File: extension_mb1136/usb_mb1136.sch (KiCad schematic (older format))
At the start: 21 parts, among them J1 Conn_01x03, J2 Conn_01x03, Q1 S9013, U1 STMPS2151MTR, U2 USBLC6-2

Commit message: update pcb
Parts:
- removed CNUSB_3: USB_B, Connector_USB:USB_B_OST_USB-B1HSxx_Horizontal, symbol Connector:USB_B
- added CNUSB_3: USB_BP, Connector_USB:USB_B_OST_USB-B1HSxx_Horizontal, symbol usb_connector_switch:USB_BP
- added D2: D, Diode_SMD:D_0805_2012Metric, symbol Device:D
- added SW1, SW2: USB_SEL, Connector_PinSocket_2.54mm:PinSocket_2x03_P2.54mm_Vertical, symbol usb_connector_switch:USB_SEL
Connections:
- net +5V: now also D2.1 (K)
- net GND: now also CNUSB_3.4 (GND), CNUSB_3.5 (Shield)
- net PA9 renamed VBUS
- new net: CNUSB_1.2 (D-), SW2.4
- new net: CNUSB_1.3 (D+), SW1.4
- new net: SW2.3, U2.4 (DMOUT)
- new net: SW1.3, U2.6 (DPOUT)
- new net: CNUSB_2.2 (D-), SW2.5
- new net: CNUSB_2.3 (D+), SW1.5
- new net: CNUSB_3.3 (D+), SW1.1
- new net: CNUSB_3.2 (D-), SW2.1
- new net: CNUSB_3.1 (VBUS), D2.2 (A)
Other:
- moved on the sheet: CNUSB_1, D1
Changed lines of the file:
@@
 L Connector:USB_OTG CNUSB_1
 U 1 1 5FBD271C
-P 10150 1900
-F 0 "CNUSB_1" H 9920 1889 50  0000 R CNN
-F 1 "USB_OTG" H 9920 1798 50  0000 R CNN
-F 2 "Connector_USB:USB_Micro-B_Molex-105017-0001" H 10300 1850 50  0001 C CNN
-F 3 " ~" H 10300 1850 50  0001 C CNN
-	1    10150 1900
+P 10150 1950
+F 0 "CNUSB_1" H 9920 1939 50  0000 R CNN
+F 1 "USB_OTG" H 9920 1848 50  0000 R CNN
+F 2 "Connector_USB:USB_Micro-B_Molex-105017-0001" H 10300 1900 50  0001 C CNN
+F 3 " ~" H 10300 1900 50  0001 C CNN
+	1    10150 1950
 	-1   0    0    -1
 $EndComp
@@
 $EndComp
 Wire Wire Line
-	9200 3000 9200 2500
-Wire Wire Line
 	10150 3400 10150 3500
 Wire Wire Line
@@
 Connection ~ 9100 2100
 Wire Wire Line
-	9100 2100 9100 1700
+	9100 2100 9100 1750
 Wire Wire Line
 	9100 2800 9100 2100
@@
 	6150 4600 6150 4700
 $Comp
-L power:GND #PWR0101
+L power:GND #PWR0104
 U 1 1 5FFB903B
 P 6150 6500
-F 0 "#PWR0101" H 6150 6250 50  0001 C CNN
+F 0 "#PWR0104" H 6150 6250 50  0001 C CNN
 F 1 "GND" H 6155 6327 50  0000 C CNN
 F 2 "" H 6150 6500 50  0001 C CNN
@@
 Wire Wire Line
 	4650 3200 4950 3200
-Wire Wire Line
-	8200 3200 8200 2500
-Wire Wire Line
-	8200 2500 9200 2500
-Connection ~ 9200 2500
-Wire Wire Line
-	9200 2500 9200 1900
-Wire Wire Line
-	9400 4150 4650 4150
 $Comp
 L Device:D D1
 U 1 1 600DB0FD
-P 9400 4450
-F 0 "D1" V 9354 4530 50  0000 L CNN
-F 1 "ESDALC6V1-1U2" V 9445 4530 50  0000 L CNN
-F 2 "Diode_SMD:D_0201_0603Metric" H 9400 4450 50  0001 C CNN
-F 3 "~" H 9400 4450 50  0001 C CNN
-	1    9400 4450
+P 9700 4450
+F 0 "D1" V 9654 4530 50  0000 L CNN
+F 1 "ESDALC6V1-1U2" V 9745 4530 50  0000 L CNN
+F 2 "Diode_SMD:D_0201_0603Metric" H 9700 4450 50  0001 C CNN
+F 3 "~" H 9700 4450 50  0001 C CNN
+	1    9700 4450
 	0    1    1    0
 $EndComp
 Wire Wire Line
-	9400 4150 9400 4300
-Connection ~ 9400 4150
+	9700 4150 9700 4300
+Connection ~ 9700 4150
 $Comp
 L power:GND #PWR0114
 U 1 1 600E78F0
-P 9400 4700
-F 0 "#PWR0114" H 9400 4450 50  0001 C CNN
-F 1 "GND" H 9405 4527 50  0000 C CNN
-F 2 "" H 9400 4700 50  0001 C CNN
-F 3 "" H 9400 4700 50  0001 C CNN
-	1    9400 4700
-	1    0    0    -1
-$EndComp
-Wire Wire Line
-	9400 4600 9400 4700
-Wire Wire Line
-	9400 2100 9400 4150
-Wire Wire Line
-	6550 3200 8200 3200
-Wire Wire Line
-	6550 3400 8350 3400
+P 9700 4700
+F 0 "#PWR0114" H 9700 4450 50  0001 C CNN
+F 1 "GND" H 9705 4527 50  0000 C CNN
+F 2 "" H 9700 4700 50  0001 C CNN
+F 3 "" H 9700 4700 50  0001 C CNN
+	1    9700 4700
+	1    0    0    -1
+$EndComp
+Wire Wire Line
+	9700 4600 9700 4700
+Wire Wire Line
+	6550 3200 7950 3200
 $Comp
 L power:GND #PWR0115
@@
 Wire Wire Line
 	4650 3400 5650 3400
-Wire Wire Line
-	9300 2000 9300 2650
-Wire Wire Line
-	8350 3400 8350 2650
-Wire Wire Line
-	8350 2650 9300 2650
-Connection ~ 9300 2650
-Wire Wire Line
-	9300 2650 9300 3100
 Wire Wire Line
 	4650 2900 7850 2900
@@
 	1    0    0    -1
 $EndComp
-$Comp
-L Connector:USB_B CNUSB_3
-U 1 1 5FFEEA84
+Wire Wire Line
+	9800 3500 10150 3500
+Connection ~ 10150 3500
+$Comp
+L power:GND #PWR0105
+U 1 1 60077159
+P 10150 3600
+F 0 "#PWR0105" H 10150 3350 50  0001 C CNN
+F 1 "GND" H 10155 3427 50  0000 C CNN
+F 2 "" H 10150 3600 50  0001 C CNN
+F 3 "" H 10150 3600 50  0001 C CNN
+	1    10150 3600
+	1    0    0    -1
+$EndComp
+Wire Wire Line
+	9100 2800 9850 2800
+Wire Wire Line
+	9850 1050 9200 1050
+Wire Wire Line
+	9200 1050 9200 2450
+Wire Wire Line
+	9200 2450 8700 2450
+Wire Wire Line
+	9300 2550 8700 2550
+Wire Wire Line
+	9850 3000 8800 3000
+Wire Wire Line
+	8800 3000 8800 2650
+Wire Wire Line
+	8800 2650 8700 2650
+Wire Wire Line
+	8400 2550 7950 2550
+Wire Wire Line
+	7950 2550 7950 3200
+Wire Wire Line
+	6550 3400 8350 3400
+Wire Wire Line
+	9850 3100 9600 3100
+Wire Wire Line
+	9600 3100 9600 3500
+Wire Wire Line
+	9600 3500 8650 3500
+Wire Wire Line
+	8650 3400 9500 3400
+Wire Wire Line
+	9500 3400 9500 2050
+Wire Wire Line
+	8650 3300 9400 3300
+Wire Wire Line
+	9400 1150 9850 1150
+Wire Wire Line
+	9400 1150 9400 3300
+Wire Wire Line
+	4650 4150 9700 4150
+$Comp
+L usb_connector_switch:USB_SEL SW1
+U 1 1 60101ABF
+P 8550 2550
+F 0 "SW1" H 8550 2875 50  0000 C CNN
+F 1 "USB_SEL" H 8550 2784 50  0000 C CNN
+F 2 "Connector_PinSocket_2.54mm:PinSocket_2x03_P2.54mm_Vertical" H 8550 2400 50  0001 C CNN
+F 3 "" H 8550 2400 50  0001 C CNN
+	1    8550 2550
+	1    0    0    -1
+$EndComp
+$Comp
+L usb_connector_switch:USB_SEL SW2
+U 1 1 601086B0
+P 8500 3400
+F 0 "SW2" H 8500 3725 50  0000 C CNN
+F 1 "USB_SEL" H 8500 3634 50  0000 C CNN
+F 2 "Connector_PinSocket_2.54mm:PinSocket_2x03_P2.54mm_Vertical" H 8500 3250 50  0001 C CNN
+F 3 "" H 8500 3250 50  0001 C CNN
+	1    8500 3400
+	1    0    0    -1
+$EndComp
+$Comp
+L power:VBUS #PWR0109
+U 1 1 5FC46E71
+P 9100 1650
+F 0 "#PWR0109" H 9100 1500 50  0001 C CNN
+F 1 "VBUS" H 9115 1823 50  0000 C CNN
+F 2 "" H 9100 1650 50  0001 C CNN
+F 3 "~" H 9100 1650 50  0001 C CNN
+	1    9100 1650
+	1    0    0    -1
+$EndComp
+Wire Wire Line
+	10250 2350 10250 2450
+Wire Wire Line
+	10250 2450 10150 2450
+Wire Wire Line
+	10150 2350 10150 2450
+Connection ~ 10150 2450
+Wire Wire Line
+	10150 2450 9800 2450
+Wire Wire Line
+	10150 3500 10150 3600
+Connection ~ 9800 2450
+Wire Wire Line
+	9800 2450 9800 3500
+Wire Wire Line
+	9700 2150 9850 2150
+Wire Wire Line
+	9700 2150 9700 4150
+Wire Wire Line
+	9850 2050 9500 2050
+Wire Wire Line
+	9850 1950 9300 1950
+Wire Wire Line
+	9300 1950 9300 2550
+Wire Wire Line
+	9850 1750 9100 1750
+Wire Wire Line
+	10250 1450 10250 1550
+Wire Wire Line
+	10250 1550 10150 1550
+Wire Wire Line
+	9800 1550 9800 2450
+Wire Wire Line
+	10150 1450 10150 1550
+Connection ~ 10150 1550
+Wire Wire Line
+	10150 1550 9800 1550
+$Comp
+L Device:D D2
+U 1 1 601DB576
+P 9550 850
+F 0 "D2" H 9550 1067 50  0000 C CNN
+F 1 "D" H 9550 976 50  0000 C CNN
+F 2 "Diode_SMD:D_0805_2012Metric" H 9550 850 50  0001 C CNN
+F 3 "~" H 9550 850 50  0001 C CNN
+	1    9550 850
+	1    0    0    -1
+$EndComp
+Wire Wire Line
+	9700 850  9850 850
+$Comp
+L power:+5V #PWR0110
+U 1 1 602126C9
+P 9250 850
+F 0 "#PWR0110" H 9250 700 50  0001 C CNN
+F 1 "+5V" V 9265 978 50  0000 L CNN
+F 2 "" H 9250 850 50  0001 C CNN
+F 3 "" H 9250 850 50  0001 C CNN
+	1    9250 850
+	0    -1   -1   0
+$EndComp
+Wire Wire Line
+	9100 1650 9100 1750
+Connection ~ 9100 1750
+Wire Wire Line
+	9250 850  9400 850
+$Comp
+L usb_connector_switch:USB_BP CNUSB_3
+U 1 1 6026EB6E
 P 10150 1050
 F 0 "CNUSB_3" H 9920 1039 50  0000 R CNN
-F 1 "USB_B" H 9920 948 50  0000 R CNN
-F 2 "Connector_USB:USB_B_OST_USB-B1HSxx_Horizontal" H 10300 1000 50  0001 C CNN
-F 3 " ~" H 10300 1000 50  0001 C CNN
+F 1 "USB_BP" H 9920 948 50  0000 R CNN
+F 2 "Connector_USB:USB_B_OST_USB-B1HSxx_Horizontal" H 10150 1500 50  0001 C CNN
+F 3 "" H 10150 1500 50  0001 C CNN
 	1    10150 1050
 	-1   0    0    -1
 $EndComp
-Wire Wire Line
-	10250 1450 10150 1450
-Wire Wire Line
-	10150 1450 9800 1450
-Wire Wire Line
-	9800 3500 10150 3500
-Connection ~ 10150 1450
-Connection ~ 10150 3500
-$Comp
-L power:GND #PWR?
-U 1 1 60077159
-P 10150 3500
-F 0 "#PWR?" H 10150 3250 50  0001 C CNN
-F 1 "GND" H 10155 3327 50  0000 C CNN
-F 2 "" H 10150 3500 50  0001 C CNN
-F 3 "" H 10150 3500 50  0001 C CNN
-	1    10150 3500
-	1    0    0    -1
-$EndComp
-Wire Wire Line
-	9800 2300 10150 2300
-Connection ~ 10150 2300
-Wire Wire Line
-	10150 2300 10250 2300
-Wire Wire Line
-	9100 1700 9850 1700
-Wire Wire Line
-	9200 1900 9850 1900
-Wire Wire Line
-	9300 2000 9850 2000
-Wire Wire Line
-	9800 1450 9800 2300
-Wire Wire Line
-	9400 2100 9850 2100
-Wire Wire Line
-	9100 2800 9850 2800
-Wire Wire Line
-	9200 3000 9850 3000
-Wire Wire Line
-	9300 3100 9850 3100
-Wire Wire Line
-	9800 2300 9800 3500
-Connection ~ 9800 2300
-Wire Wire Line
-	9100 850  9850 850
-Connection ~ 9100 1700
-Wire Wire Line
-	9100 850  9100 1700
-Wire Wire Line
-	9200 1900 9200 1050
-Wire Wire Line
-	9200 1050 9850 1050
-Connection ~ 9200 1900
-Wire Wire Line
-	9300 2000 9300 1150
-Wire Wire Line
-	9300 1150 9850 1150
-Connection ~ 9300 2000
 $EndSCHEMATC

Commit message: update pcb
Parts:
- D2: footprint Diode_SMD:D_0805_2012Metric -> Diode_SMD:D_0805_2012Metric_Pad1.15x1.40mm_HandSolder
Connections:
- net +5V: no longer D2.1 (K), U1.2 (IN), U1.3 (IN)
- new net +5VD: D2.1 (K), U1.2 (IN), U1.3 (IN)
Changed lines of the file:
@@
 	6000 1650 6100 1650
 $Comp
-L power:+5V #PWR0107
+L power:+5VD #PWR0107
 U 1 1 6008E133
 P 6000 1650
 F 0 "#PWR0107" H 6000 1500 50  0001 C CNN
-F 1 "+5V" V 6015 1778 50  0000 L CNN
+F 1 "+5VD" V 6015 1778 50  0000 L CNN
 F 2 "" H 6000 1650 50  0001 C CNN
 F 3 "" H 6000 1650 50  0001 C CNN
@@
 F 0 "D2" H 9550 1067 50  0000 C CNN
 F 1 "D" H 9550 976 50  0000 C CNN
-F 2 "Diode_SMD:D_0805_2012Metric" H 9550 850 50  0001 C CNN
+F 2 "Diode_SMD:D_0805_2012Metric_Pad1.15x1.40mm_HandSolder" H 9550 850 50  0001 C CNN
 F 3 "~" H 9550 850 50  0001 C CNN
 	1    9550 850
@@
 	9700 850  9850 850
 $Comp
-L power:+5V #PWR0110
+L power:+5VD #PWR0110
 U 1 1 602126C9
 P 9250 850
 F 0 "#PWR0110" H 9250 700 50  0001 C CNN
-F 1 "+5V" V 9265 978 50  0000 L CNN
+F 1 "+5VD" V 9265 978 50  0000 L CNN
 F 2 "" H 9250 850 50  0001 C CNN
 F 3 "" H 9250 850 50  0001 C CNN

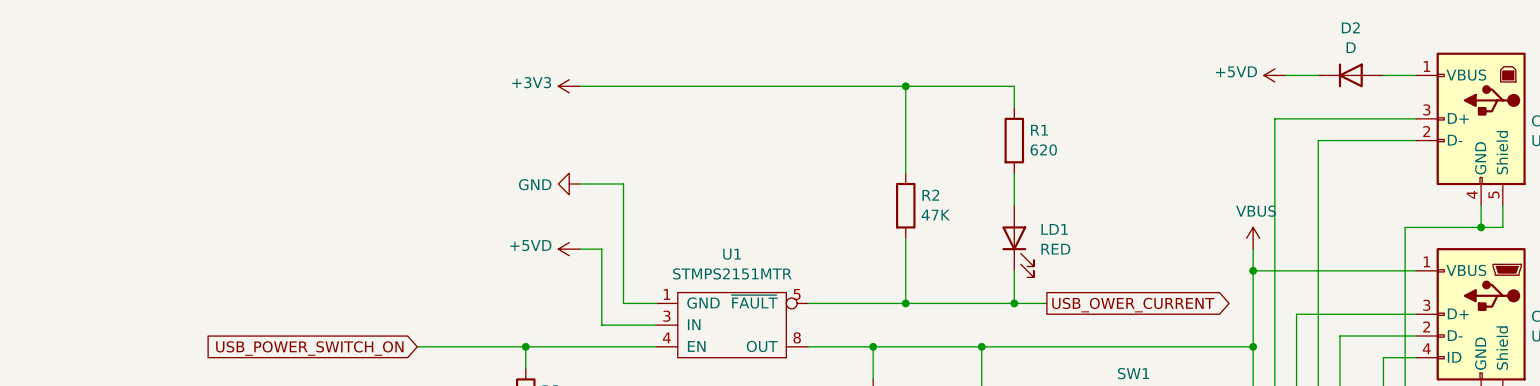
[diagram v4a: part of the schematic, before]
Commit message: change footprint for D2,D3
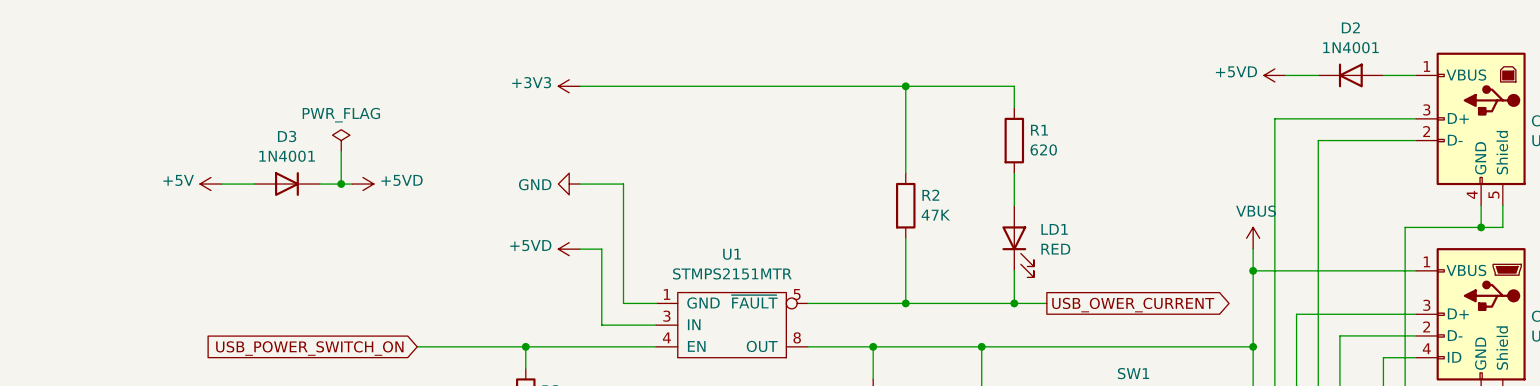
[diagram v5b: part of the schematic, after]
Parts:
- added D3: 1N4001, Diode_SMD:D_SOD-323_HandSoldering, symbol Device:D
- D2: value D -> 1N4001; footprint Diode_SMD:D_0805_2012Metric_Pad1.15x1.40mm_HandSolder -> Diode_SMD:D_SOD-323_HandSoldering
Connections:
- net +5V: now also D3.2 (A)
- net +5VD: now also D3.1 (K)
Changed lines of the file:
@@
 P 9550 850
 F 0 "D2" H 9550 1067 50  0000 C CNN
-F 1 "D" H 9550 976 50  0000 C CNN
-F 2 "Diode_SMD:D_0805_2012Metric_Pad1.15x1.40mm_HandSolder" H 9550 850 50  0001 C CNN
+F 1 "1N4001" H 9550 976 50  0000 C CNN
+F 2 "Diode_SMD:D_SOD-323_HandSoldering" H 9550 850 50  0001 C CNN
 F 3 "~" H 9550 850 50  0001 C CNN
 	1    9550 850
@@
 	-1   0    0    -1
 $EndComp
+$Comp
+L Device:D D3
+U 1 1 600332DD
+P 4650 1350
+AR Path="/5FBD0FDB/600332DD" Ref="D3"  Part="1"
+AR Path="/5FBD0F73/600332DD" Ref="D?"  Part="1"
+F 0 "D3" H 4650 1567 50  0000 C CNN
+F 1 "1N4001" H 4650 1476 50  0000 C CNN
+F 2 "Diode_SMD:D_SOD-323_HandSoldering" H 4650 1350 50  0001 C CNN
+F 3 "~" H 4650 1350 50  0001 C CNN
+	1    4650 1350
+	-1   0    0    -1
+$EndComp
+$Comp
+L power:+5V #PWR?
+U 1 1 600332E3
+P 4350 1350
+AR Path="/5FBD0F73/600332E3" Ref="#PWR?"  Part="1"
+AR Path="/5FBD0FDB/600332E3" Ref="#PWR0116"  Part="1"
+F 0 "#PWR0116" H 4350 1200 50  0001 C CNN
+F 1 "+5V" V 4365 1478 50  0000 L CNN
+F 2 "" H 4350 1350 50  0001 C CNN
+F 3 "" H 4350 1350 50  0001 C CNN
+	1    4350 1350
+	0    -1   -1   0
+$EndComp
+$Comp
+L power:+5VD #PWR?
+U 1 1 600332E9
+P 4950 1350
+AR Path="/5FBD0F73/600332E9" Ref="#PWR?"  Part="1"
+AR Path="/5FBD0FDB/600332E9" Ref="#PWR0117"  Part="1"
+F 0 "#PWR0117" H 4950 1200 50  0001 C CNN
+F 1 "+5VD" V 4965 1478 50  0000 L CNN
+F 2 "" H 4950 1350 50  0001 C CNN
+F 3 "" H 4950 1350 50  0001 C CNN
+	1    4950 1350
+	0    1    -1   0
+$EndComp
+Wire Wire Line
+	4350 1350 4500 1350
+$Comp
+L power:PWR_FLAG #FLG?
+U 1 1 600332F0
+P 4900 1200
+AR Path="/5FBD0F73/600332F0" Ref="#FLG?"  Part="1"
+AR Path="/5FBD0FDB/600332F0" Ref="#FLG0104"  Part="1"
+F 0 "#FLG0104" H 4900 1275 50  0001 C CNN
+F 1 "PWR_FLAG" H 4900 1373 50  0000 C CNN
+F 2 "" H 4900 1200 50  0001 C CNN
+F 3 "~" H 4900 1200 50  0001 C CNN
+	1    4900 1200
+	1    0    0    -1
+$EndComp
+Wire Wire Line
+	4800 1350 4900 1350
+Wire Wire Line
+	4900 1200 4900 1350
+Connection ~ 4900 1350
+Wire Wire Line
+	4900 1350 4950 1350
 $EndSCHEMATC

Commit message: change footprint for SW1 SW2
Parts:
- SW1, SW2: footprint Connector_PinSocket_2.54mm:PinSocket_2x03_P2.54mm_Vertical -> Connector_PinHeader_2.54mm:PinHeader_2x03_P2.54mm_Vertical
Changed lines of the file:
@@
 F 0 "SW1" H 8550 2875 50  0000 C CNN
 F 1 "USB_SEL" H 8550 2784 50  0000 C CNN
-F 2 "Connector_PinSocket_2.54mm:PinSocket_2x03_P2.54mm_Vertical" H 8550 2400 50  0001 C CNN
+F 2 "Connector_PinHeader_2.54mm:PinHeader_2x03_P2.54mm_Vertical" H 8550 2400 50  0001 C CNN
 F 3 "" H 8550 2400 50  0001 C CNN
 	1    8550 2550
@@
 F 0 "SW2" H 8500 3725 50  0000 C CNN
 F 1 "USB_SEL" H 8500 3634 50  0000 C CNN
-F 2 "Connector_PinSocket_2.54mm:PinSocket_2x03_P2.54mm_Vertical" H 8500 3250 50  0001 C CNN
+F 2 "Connector_PinHeader_2.54mm:PinHeader_2x03_P2.54mm_Vertical" H 8500 3250 50  0001 C CNN
 F 3 "" H 8500 3250 50  0001 C CNN
 	1    8500 3400

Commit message: chande footprint for C1. update pcb
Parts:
- C1: footprint Capacitor_SMD:C_1206_3216Metric -> Capacitor_SMD:C_1206_3216Metric_Pad1.33x1.80mm_HandSolder
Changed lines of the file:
@@
 F 0 "C1" H 7468 2446 50  0000 L CNN
 F 1 "4.7uF" H 7468 2355 50  0000 L CNN
-F 2 "Capacitor_SMD:C_1206_3216Metric" H 7388 2250 50  0001 C CNN
+F 2 "Capacitor_SMD:C_1206_3216Metric_Pad1.33x1.80mm_HandSolder" H 7388 2250 50  0001 C CNN
 F 3 "~" H 7350 2400 50  0001 C CNN
 	1    7350 2400

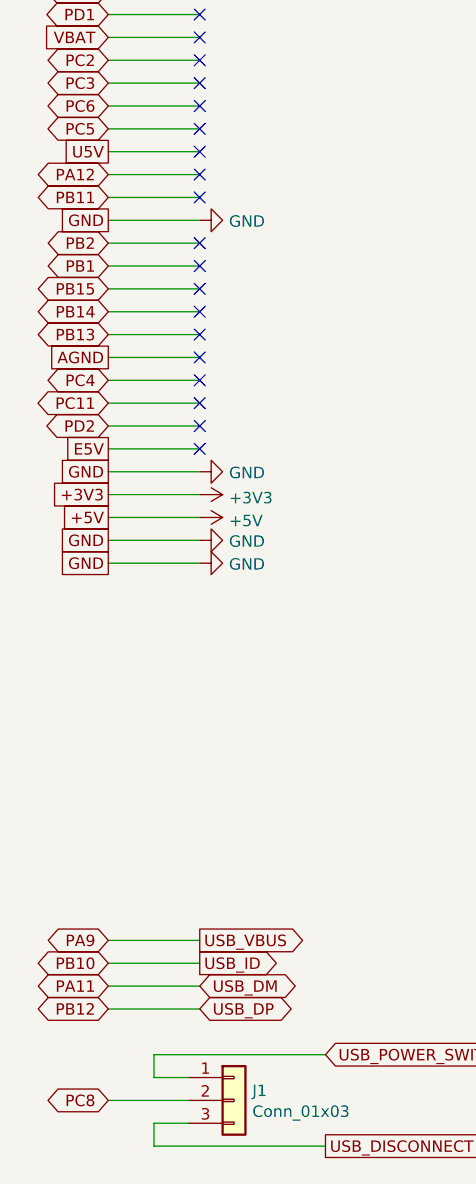
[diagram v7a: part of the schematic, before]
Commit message: fix error USB_DP
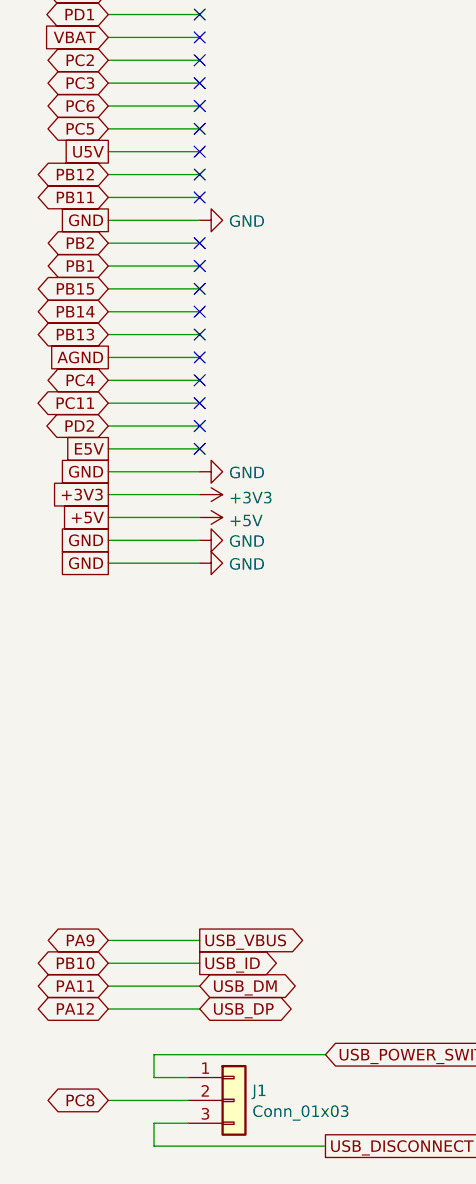
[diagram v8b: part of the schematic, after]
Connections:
- net PA12: now also R9.1, U2.1 (DPIN)
- net PB12: no longer R9.1, U2.1 (DPIN)
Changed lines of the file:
@@
 PC5
 Text GLabel 900  2650 0    50   BiDi ~ 0
-PA12
+PB12
 Text GLabel 900  2750 0    50   BiDi ~ 0
 PB11
@@
 	1300 6300 900  6300
 Text GLabel 900  6300 0    50   BiDi ~ 0
-PB12
+PA12
 Text GLabel 900  6200 0    50   BiDi ~ 0
 PA11
